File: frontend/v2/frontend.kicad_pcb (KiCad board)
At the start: 2 copper layers, 41.5 x 49.9 mm, 122 parts, among them CN1 EDGE, CN2 BREAKOUT, CN3 TXL, CN4 AGND, CN5 AGND, J1 0, J2 0, P1 BNC, P2 BNC, T1 4:1, T2 8:1

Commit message: Updated Schematic, floorplanning
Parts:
- removed CN4, CN5: AGND, HERMESLITE:JUMPER
- removed G*** (x2): OSHW-logo_silkscreen-front_2mm, OSHW:OSHW-logo_silkscreen-front_2mm
- removed HOLE (x98): VAL**, HERMESLITE:HOLE
- removed J1, J2: 0, HERMESLITE:JUMPER
- removed PROTOEDGE12L: VAL**, HERMESLITE:PROTOEDGE12L
- removed PROTOEDGE12S: VAL**, HERMESLITE:PROTOEDGE12S
- added C10: 0.1uF, Capacitors_SMD:C_0805, F.Cu at (113.8, 103.5)
- added C11: 0pF, Capacitors_SMD:C_0805, B.Cu at (122.2, 108.0)
- added C12: 0pF, Capacitors_SMD:C_0805, B.Cu at (125.2, 109.5)
- added C13: 0pF, Capacitors_SMD:C_0805, B.Cu at (129.2, 107.2)
- added C14: 0pF, Capacitors_SMD:C_0805, B.Cu at (124.8, 106.8)
- added C15: 0pF, Capacitors_SMD:C_0805, B.Cu at (131.8, 108.0)
- added C5: 8.4pF, Capacitors_SMD:C_0805, B.Cu at (116.2, 93.2)
- added C6: 75pF, Capacitors_SMD:C_0805, B.Cu at (117.8, 93.8)
- added C7: 0.1uF, Capacitors_SMD:C_0805, B.Cu at (108.0, 99.0)
- added C8: 0.1uF, Capacitors_SMD:C_0805, B.Cu at (105.2, 107.2)
- added C9: 0.1uF, Capacitors_SMD:C_0805, F.Cu at (111.8, 105.5)
- added L1: 150nH, HERMESLITE:inductor, F.Cu at (117.7, 94.5)
- added L2: 270nH, HERMESLITE:inductor, F.Cu at (124.7, 93.2)
- added L3: 0H, HERMESLITE:inductor, F.Cu at (131.8, 91.6)
- added L4: 0nH, HERMESLITE:inductor, F.Cu at (124.8, 106.8)
- added L5: 0nH, HERMESLITE:inductor, F.Cu at (131.8, 108.0)
- added P3: SMA/BNC/HDR, HERMESLITE:rfconnector, F.Cu at (140.8, 110.1)
- added P4: CONN_01X02, Capacitors_SMD:C_0805, F.Cu at (101.2, 95.8)
- added R2: DNI, Capacitors_SMD:C_0805, B.Cu at (106.0, 93.0)
- added R3: DNI, Capacitors_SMD:C_0805, B.Cu at (125.2, 97.8)
- added R4: 0, Capacitors_SMD:C_0805, B.Cu at (129.8, 96.8)
- added R5: 87, Capacitors_SMD:C_0805, B.Cu at (134.5, 97.8)
- added R6: 43, Capacitors_SMD:C_0805, B.Cu at (132.5, 95.8)
- added R7: 2.2K, Capacitors_SMD:C_0805, B.Cu at (132.5, 92.2)
- added R8: 76, Capacitors_SMD:C_0805, B.Cu at (134.5, 93.8)
- added U1: PE4259, HERMESLITE:pe4259, F.Cu at (115.0, 98.5)
- added U2: PE4259, HERMESLITE:pe4259, F.Cu at (118.0, 102.0)
- added U3: PE4259, HERMESLITE:pe4259, F.Cu at (118.0, 104.8)
- added U4: PE4259, HERMESLITE:pe4259, F.Cu at (118.0, 107.5)
- added U5: PE4259, HERMESLITE:pe4259, F.Cu at (112.2, 95.2)
- added U6: ULN2803, HERMESLITE:PSOP-18, F.Cu at (108.2, 86.0)
- C1: value 0.1 uF -> 110pF; footprint SMD_Packages:SMD-0805 -> Capacitors_SMD:C_0805
- C2: value 0.1 uF -> 220pF; footprint SMD_Packages:SMD-0805 -> Capacitors_SMD:C_0805
- C3: value 0.1 uF -> 160pF; footprint SMD_Packages:SMD-0805 -> Capacitors_SMD:C_0805
- C4: value 0.1 uF -> DNI; footprint SMD_Packages:SMD-0805 -> Capacitors_SMD:C_0805
- CN2: value BREAKOUT -> RELAYCNT; footprint HERMESLITE:BREAKOUT -> HERMESLITE:10pin
- CN3: value TXL -> RXCNT; footprint HERMESLITE:JUMPER -> HERMESLITE:4pinmid
- D1: moved to F.Cu
- FB1, R1: footprint SMD_Packages:SMD-0805 -> Capacitors_SMD:C_0805
- P1, P2: value BNC -> SMA/BNC/HDR; footprint HERMESLITE:BNCRA -> HERMESLITE:rfconnector
- T1: value 4:1 -> 1:1; footprint HERMESLITE:TRANSFREV -> HERMESLITE:TRANSFSMT
- T2: value 8:1 -> 8:1 Z; footprint HERMESLITE:TRANSFREV -> HERMESLITE:TRANSFSMT
- moved P2 39.5 mm to (140.8, 97.4)
- moved P1 35.7 mm to (140.8, 84.7)
- moved CN2 34.7 mm to (128.5, 67.1), turned to 90 degrees
- moved C4 29.1 mm to (131.2, 90.0), turned to 180 degrees
- moved CN3 20.9 mm to (112.0, 113.5)
- moved C3 17.3 mm to (125.2, 96.0), turned to 180 degrees
- moved T1 16.4 mm to (107.2, 98.2), turned to 90 degrees
- moved R1 14.8 mm to (106.0, 91.2), turned to 0 degrees
- moved C2 13.2 mm to (122.0, 93.7), turned to 270 degrees
- moved FB1 8.72 mm to (107.0, 95.8), turned to 90 degrees
- moved C1 4.75 mm to (118.7, 96.5), turned to 0 degrees
- moved D1 3.15 mm to (112.8, 108.2)
- moved T2 1.66 mm to (105.8, 107.0), turned to 90 degrees
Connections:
- C3 pad 2: Net-(C3-Pad2) -> GND
- C4 pad 2: Net-(C3-Pad1) -> GND
- CN1 pad A12: Net-(CN1-PadA11) -> Net-(CN1-PadA12)
- CN1 pad A13: Net-(CN1-PadA13) -> 5V
- CN1 pad A14: Net-(CN1-PadA13) -> 5V
- CN1 pad A15: Net-(CN1-PadA15) -> 3V
- CN1 pad A16: Net-(CN1-PadA15) -> 3V
- CN1 pad A17: Net-(CN1-PadA17) -> GNDREF
- CN1 pad A18: Net-(CN1-PadA17) -> GNDREF
- CN2 pad 1: Net-(CN1-PadB14) -> Net-(CN2-Pad1)
- CN2 pad 10: Net-(CN1-PadB18) -> GNDREF
- CN2 pad 2: Net-(CN1-PadB13) -> Net-(CN2-Pad2)
- CN2 pad 3: Net-(CN1-PadB12) -> Net-(CN2-Pad3)
- CN2 pad 4: Net-(CN1-PadB11) -> Net-(CN2-Pad4)
- CN2 pad 5: Net-(CN1-PadA13) -> Net-(CN2-Pad5)
- CN2 pad 6: Net-(CN1-PadA11) -> Net-(CN2-Pad6)
- CN2 pad 7: Net-(CN1-PadB15) -> Net-(CN2-Pad7)
- CN2 pad 8: Net-(CN1-PadB16) -> Net-(CN2-Pad8)
- CN2 pad 9: Net-(CN1-PadB17) -> Net-(CN2-Pad9)
- CN3 pad 1: Net-(CN1-PadB9) -> TR
- CN3 pad 2: Net-(CN1-PadB8) -> TAP
- D1 pad 1: Net-(C3-Pad1) -> Net-(C10-Pad2)
- D1 pad 2: Net-(D1-Pad2) -> GND
- FB1 pad 1: Net-(CN1-PadA13) -> Net-(C7-Pad1)
- P1 pad 1: Net-(P1-Pad1) -> Net-(C4-Pad1)
- P1 pad 2: Net-(J1-Pad1) -> GND
- P2 pad 1: Net-(C4-Pad1) -> Net-(P2-Pad1)
- P2 pad 2: Net-(D1-Pad2) -> GND
- R1 pad 1: Net-(C1-Pad1) -> 3V
- T1 pad 1: Net-(P1-Pad1) -> Net-(CN1-PadB6)
- T1 pad 2: Net-(J1-Pad1) -> Net-(C7-Pad1)
- T1 pad 3: Net-(C1-Pad1) -> Net-(CN1-PadB5)
- T1 pad 4: Net-(CN1-PadB5) -> GND
- T1 pad 5: Net-(CN1-PadB6) -> Net-(T1-Pad5)
- T2 pad 1: Net-(C3-Pad2) -> Net-(CN1-PadB3)
- T2 pad 2: Net-(D1-Pad2) -> Net-(C8-Pad1)
- T2 pad 3: Net-(C2-Pad1) -> Net-(CN1-PadB2)
- T2 pad 4: Net-(CN1-PadB2) -> GND
- T2 pad 5: Net-(CN1-PadB3) -> Net-(C9-Pad2)
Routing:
- net Net-(D1-Pad2): track 40.4 -> 0.00 mm
- net Net-(J1-Pad1): track 35.6 -> 0.00 mm
- net Net-(CN1-PadA13): track 34.9 -> 0.00 mm, vias 1 -> 0
- net GND: track 65.5 -> 31.0 mm, vias 3 -> 0
- net Net-(CN1-PadB6): track 32.1 -> 0.00 mm
- net Net-(CN1-PadB5): track 29.7 -> 0.00 mm
- net Net-(CN1-PadA11): track 28.9 -> 0.00 mm
- net Net-(CN1-PadA17): track 26.7 -> 0.00 mm
- net Net-(CN1-PadA15): track 23.7 -> 0.00 mm
- net Net-(CN1-PadB3): track 17.2 -> 0.00 mm
- net Net-(CN1-PadB11): track 16.7 -> 0.00 mm
- net Net-(CN1-PadB18): track 16.3 -> 0.00 mm
- net Net-(CN1-PadB17): track 13.7 -> 0.00 mm
- net Net-(CN1-PadB12): track 13.5 -> 0.00 mm
- net Net-(CN1-PadB2): track 13.5 -> 0.00 mm
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- removed copper zone on B.Cu, net GND
- removed copper zone on F.Cu, net GND
- removed copper zone on B.Cu, net Net-(D1-Pad2)
- removed copper zone on F.Cu, net Net-(D1-Pad2)
- removed copper zone on B.Cu, net Net-(J1-Pad1)
- removed copper zone on F.Cu, net Net-(J1-Pad1)
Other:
- board text added: "Hermes-Lite Basic Frontend 1.2"
- board text removed: "Hermes-Lite Basic Frontend 1.0"
- board text removed: "©2014 SofterHardware"

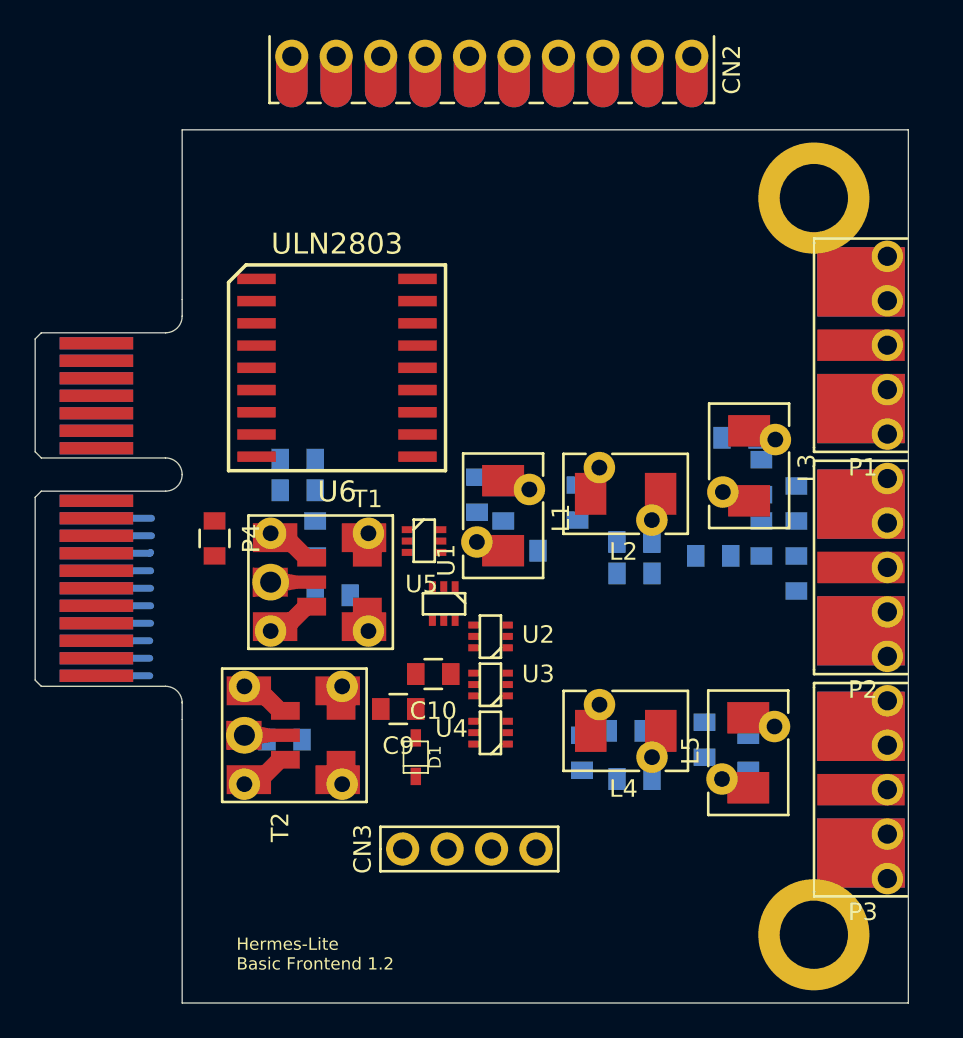
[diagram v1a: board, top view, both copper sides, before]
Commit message: New frontend board
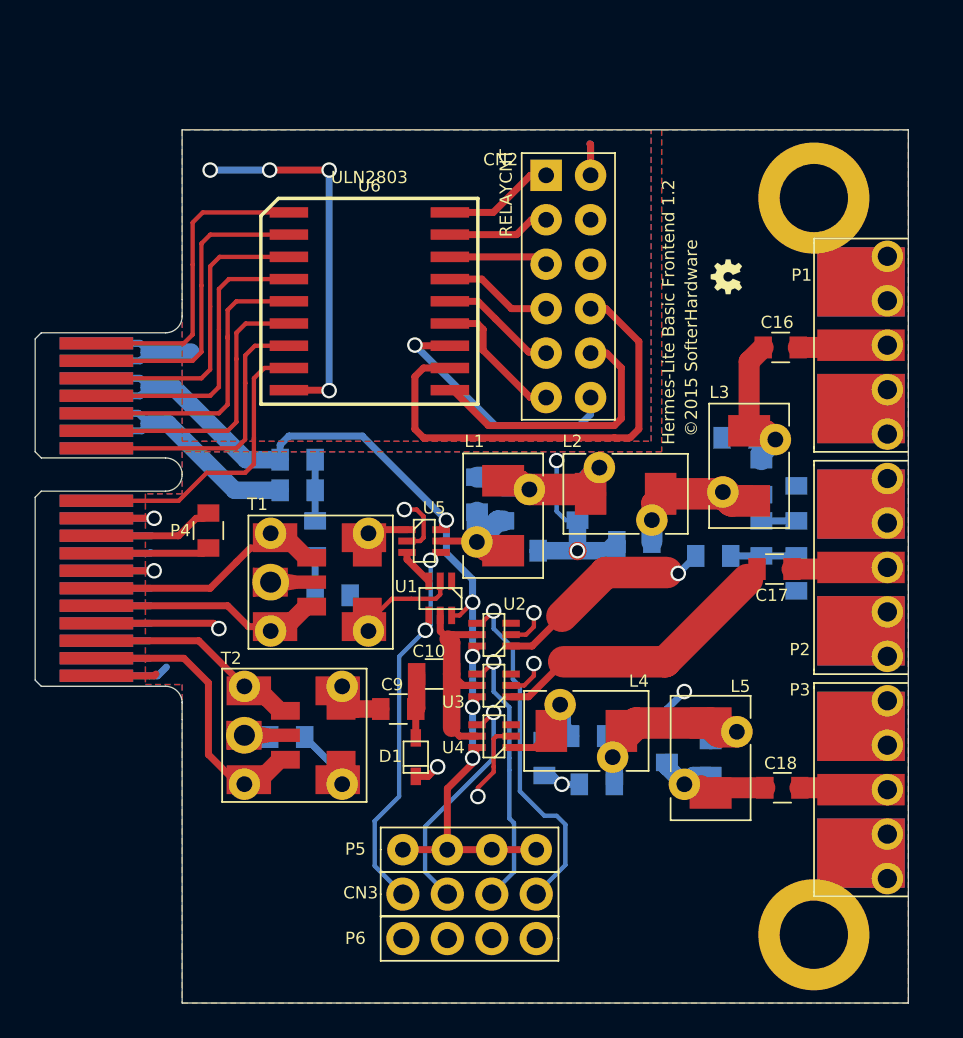
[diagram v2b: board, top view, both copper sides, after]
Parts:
- added C16: 0.1uF, Capacitors_SMD:C_0805, F.Cu at (133.6, 84.8)
- added C17: 0.1uF, Capacitors_SMD:C_0805, F.Cu at (133.2, 97.5)
- added C18: 0.1uF, Capacitors_SMD:C_0805, F.Cu at (133.7, 110.0)
- added G***: OSHW-logo_silkscreen-front_2mm, HERMESLITE:OSHW-logo_silkscreen-front_2mm, F.Cu at (130.5, 80.8)
- added G***: OSHW-logo_silkscreen-back_2mm, HERMESLITE:OSHW-logo_silkscreen-back_2mm, B.Cu at (130.5, 80.8)
- added P5: CONN_01X04, HERMESLITE:4pinmid, F.Cu at (112.0, 113.5)
- added P6: CONN_01X04, HERMESLITE:4pinmid, F.Cu at (119.6, 118.6)
- C11, C13: value 0pF -> 100pF
- C12: value 0pF -> 180pF
- C14, C15: value 0pF -> DNI
- CN2: footprint HERMESLITE:10pin -> HERMESLITE:BREAKOUT
- L4, L5: value 0nH -> 390nH
- moved CN2 11.5 mm to (120.2, 75.0), turned to 270 degrees
- moved U6 4.23 mm to (110.1, 82.2)
- moved CN3 2.58 mm to (112.0, 116.1)
- moved L4 2.25 mm to (122.5, 106.8)
- moved C11 2.17 mm to (120.1, 108.3)
- moved C12 2.17 mm to (123.1, 109.8)
- moved C13 2.17 mm to (127.1, 107.5)
- moved C14 2.17 mm to (122.6, 107.0)
- moved C15 2.17 mm to (129.6, 108.3)
- moved L5 2.17 mm to (129.6, 108.3)
- moved P4 0.57 mm to (100.9, 95.3)
- moved U1 0.36 mm to (114.8, 98.2)
- moved U4 0.28 mm to (118.2, 107.7)
- moved U2 0.22 mm to (118.2, 101.9)
- moved C8 0.21 mm to (105.4, 107.1)
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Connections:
- C4 pad 1: Net-(C4-Pad1) -> Net-(C16-Pad1)
- CN2 pad 10: GNDREF -> Net-(CN2-Pad10)
- CN2 pad 2: Net-(CN2-Pad2) -> GNDREF
- CN2 pad 4: Net-(CN2-Pad4) -> GNDREF
- CN2 pad 6: Net-(CN2-Pad6) -> GNDREF
- CN3 pad 2: TAP -> RX3
- CN3 pad 4: RX3 -> TAP
- L3 pad 2: Net-(C4-Pad1) -> Net-(C16-Pad1)
- P1 pad 1: Net-(C4-Pad1) -> Net-(C16-Pad2)
- P2 pad 1: Net-(P2-Pad1) -> Net-(C17-Pad2)
- P3 pad 1: Net-(C13-Pad1) -> Net-(C18-Pad2)
- R7 pad 2: Net-(C4-Pad1) -> Net-(C16-Pad1)
- U3 pad 1: Net-(P2-Pad1) -> Net-(C17-Pad1)
- U6 pad 10: Net-(CN2-Pad9) -> Net-(CN2-Pad10)
- U6 pad 12: Net-(CN2-Pad7) -> Net-(CN2-Pad12)
- U6 pad 13: Net-(CN2-Pad6) -> Net-(CN2-Pad11)
- U6 pad 14: Net-(CN2-Pad5) -> Net-(CN2-Pad9)
- U6 pad 15: Net-(CN2-Pad4) -> Net-(CN2-Pad7)
- U6 pad 16: Net-(CN2-Pad3) -> Net-(CN2-Pad5)
- U6 pad 17: Net-(CN2-Pad2) -> Net-(CN2-Pad3)
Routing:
- net GND: track 31.0 -> 95.5 mm, vias 0 -> 12
- net 3V: track 0.00 -> 60.3 mm, vias 0 -> 5
- net GNDREF: track 0.00 -> 34.2 mm, vias 0 -> 4
- net Net-(CN2-Pad8): track 0.00 -> 27.0 mm
- net TR: track 0.00 -> 22.8 mm, vias 0 -> 2
- net TAP: track 0.00 -> 20.2 mm, vias 0 -> 1
- net Net-(CN1-PadB18): track 0.00 -> 17.8 mm
- net Net-(CN1-PadB17): track 0.00 -> 17.6 mm
- net Net-(CN1-PadB16): track 0.00 -> 17.3 mm
- net Net-(CN1-PadB11): track 0.00 -> 17.1 mm
- net Net-(C17-Pad1): track 0.00 -> 17.1 mm
- net Net-(CN1-PadB15): track 0.00 -> 17.0 mm
- net Net-(CN1-PadB14): track 0.00 -> 16.9 mm
- net Net-(CN1-PadB13): track 0.00 -> 16.5 mm
- net Net-(CN1-PadB12): track 0.00 -> 16.3 mm
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- added copper zone on B.Cu, net GND
- added copper zone on F.Cu, net GND
- added copper zone on B.Cu, net GNDREF
- added copper zone on F.Cu, net GNDREF
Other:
- board text added: "©2015 SofterHardware"
